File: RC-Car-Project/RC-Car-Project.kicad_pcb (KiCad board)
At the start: 4 copper layers, 80 x 120 mm, 140 parts, among them J1 Conn_01x02_Pin, J10 ANT_IF, J11 Conn_01x02, J12 Conn_01x02, J13 RF_IF, J15 USB4120-03-C_REVA, J2 Conn_01x02_Pin, J3 Conn_01x02_Pin, J4 Conn_01x02_Pin, J5 MCU_IF, J6 Conn_01x02, J7 Conn_01x02, J8 Conn_01x02, J9 Conn_02x09_Odd_Even, Q1 BTN8982TA, Q2 BTN8982TA, Q3 BTN8982TA, Q4 BTN8982TA, Q5 2N7002E, Q6 2N7002E, Q7 PMOS, SW1 SW_Push, U1 LMR16020PDDAR, U11 LMR16030PDDA, U3 STM32H743VGTx, U4 USBLC6-2SC6, U7 INA229AQDGSRQ1, U8 ADC082S021CIMM/NOPB, U9 SN74HC244PWR, Y1 Crystal

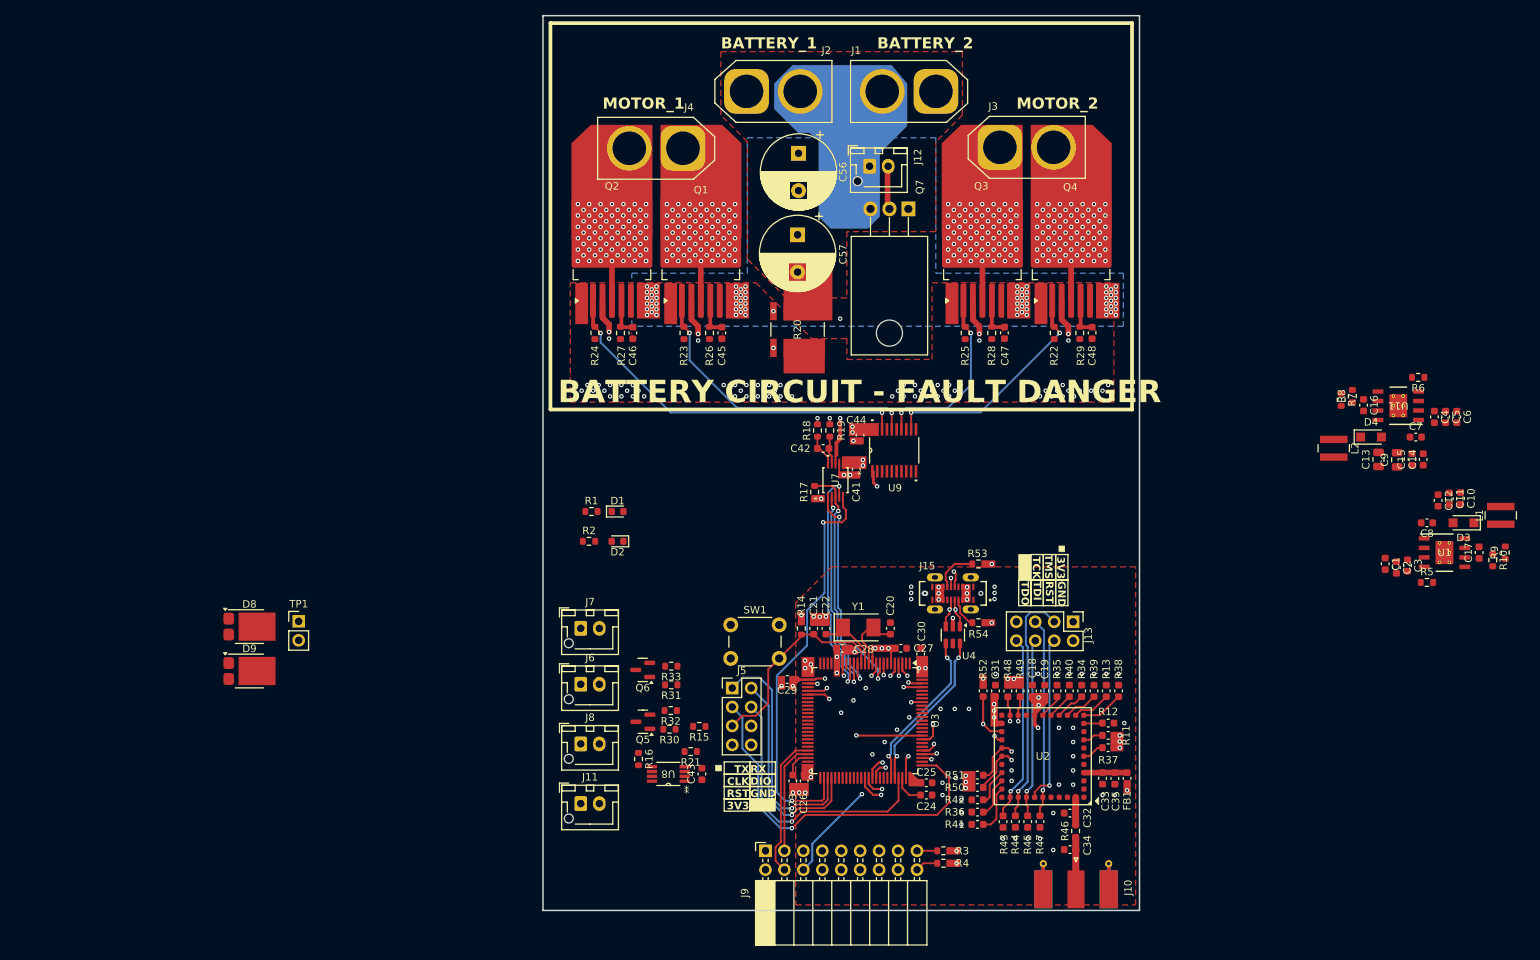
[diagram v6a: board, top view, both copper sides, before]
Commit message: Finished prelim. Car and added screw holes
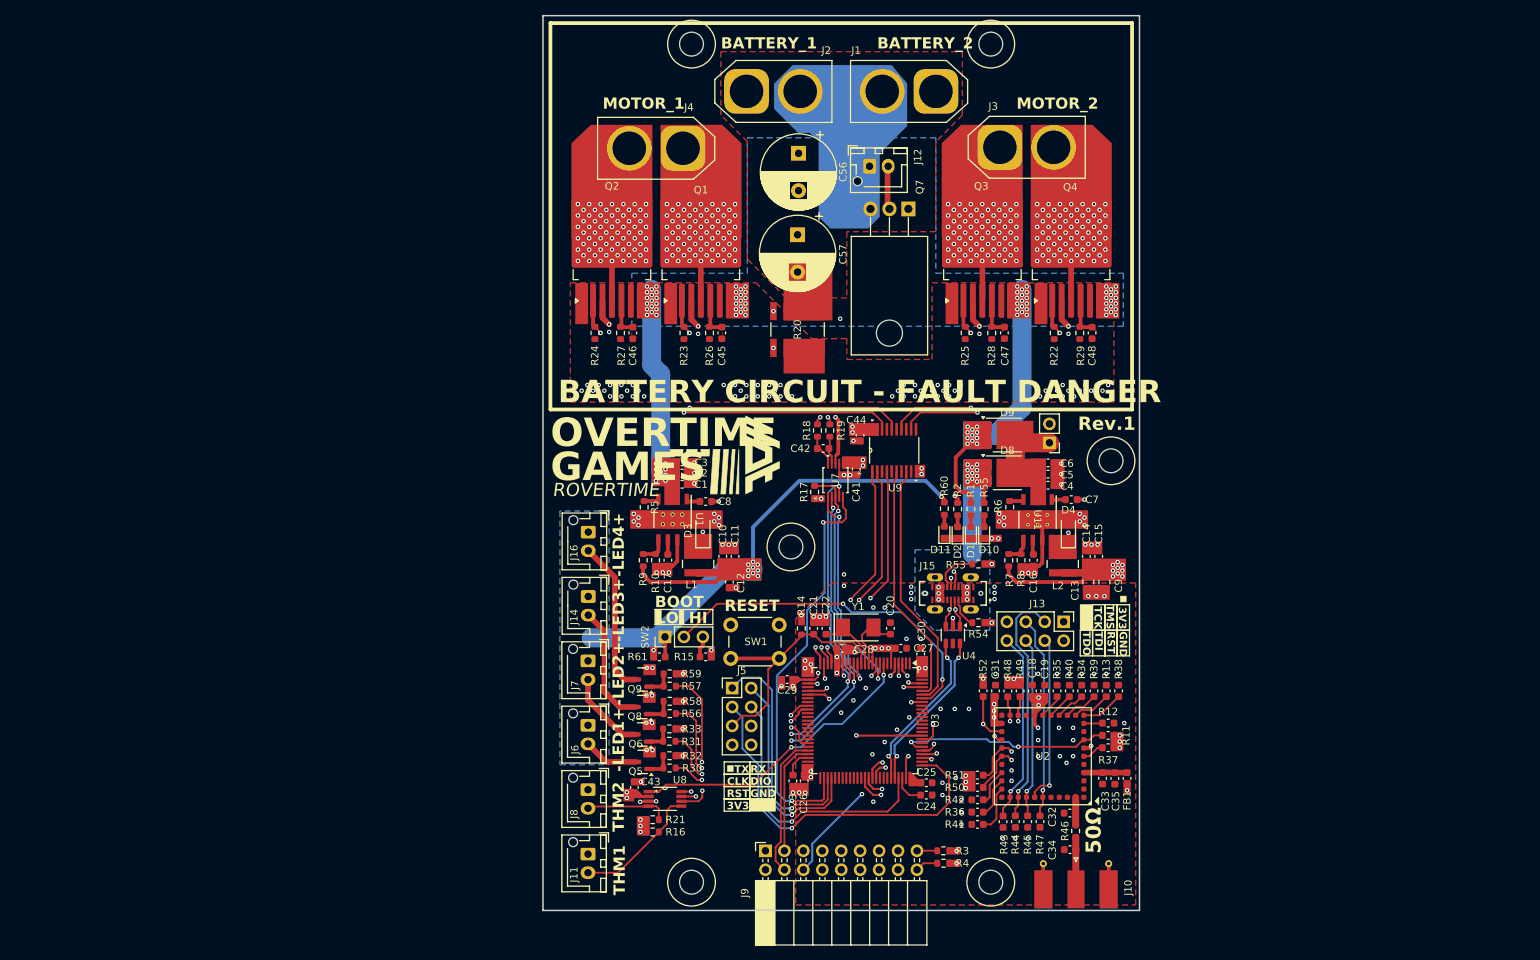
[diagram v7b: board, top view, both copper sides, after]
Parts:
- added D10: LED, LED_SMD:LED_0603_1608Metric, F.Cu at (169.2, 109.3)
- added D11: LED, LED_SMD:LED_0603_1608Metric, F.Cu at (163.8, 109.3)
- added J14: Conn_01x02, Connector_JST:JST_XH_B2B-XH-AM_1x02_P2.50mm_Vertical, F.Cu at (116.1, 117.9)
- added J16: Conn_01x02, Connector_JST:JST_XH_B2B-XH-AM_1x02_P2.50mm_Vertical, F.Cu at (116.1, 109.3)
- added Q8: 2N7002E, Package_TO_SOT_SMD:SOT-23, F.Cu at (123.3, 132.7)
- added Q9: 2N7002E, Package_TO_SOT_SMD:SOT-23, F.Cu at (123.4, 129.0)
- added R55: 220ohm, Resistor_SMD:R_0603_1608Metric, F.Cu at (169.2, 106.2)
- added R56: 100, Resistor_SMD:R_0603_1608Metric, F.Cu at (127.0, 133.6)
- added R57: 100, Resistor_SMD:R_0603_1608Metric, F.Cu at (127.0, 129.9)
- added R58: 10k, Resistor_SMD:R_0603_1608Metric, F.Cu at (127.0, 132.0)
- added R59: 10k, Resistor_SMD:R_0603_1608Metric, F.Cu at (127.0, 128.3)
- added R60: 1.5kohm, Resistor_SMD:R_0603_1608Metric, F.Cu at (163.8, 106.1)
- added R61: 10k, Capacitor_SMD:C_0603_1608Metric, F.Cu at (125.6, 126.0)
- added REF**: MountingHole_3.2mm_M3, MountingHole:MountingHole_3.2mm_M3, F.Cu at (143.3, 111.3)
- added REF**: Overtime_Small, _LOGOS:Overtime_Small, F.Cu at (138.6, 99.1)
- added REF**: MountingHole_3.2mm_M3, MountingHole:MountingHole_3.2mm_M3, F.Cu at (170.1, 43.8)
- added REF**: MountingHole_3.2mm_M3, MountingHole:MountingHole_3.2mm_M3, F.Cu at (170.1, 156.2)
- added REF**: MountingHole_3.2mm_M3, MountingHole:MountingHole_3.2mm_M3, F.Cu at (129.9, 156.2)
- added REF**: MountingHole_3.2mm_M3, MountingHole:MountingHole_3.2mm_M3, F.Cu at (129.9, 43.8)
- added REF**: MountingHole_3.2mm_M3, MountingHole:MountingHole_3.2mm_M3, F.Cu at (186.2, 99.7)
- added SW2: SW_SPDT, Connector_PinHeader_2.54mm:PinHeader_1x03_P2.54mm_Vertical, F.Cu at (126.4, 123.3)
- R15: footprint Resistor_SMD:R_0603_1608Metric -> Capacitor_SMD:C_0603_1608Metric
- moved R9 115.6 mm to (123.4, 113.0), turned to -90 degrees
- moved R10 112.3 mm to (125.1, 113.0), turned to 90 degrees
- moved C17 108.8 mm to (126.7, 113.0), turned to -90 degrees
- moved L1 107.8 mm to (130.8, 113.5), turned to -90 degrees
- moved D9 106.5 mm to (172.3, 96.2)
- moved R5 105.5 mm to (123.6, 105.9), turned to -90 degrees
- moved D8 103.7 mm to (172.3, 101.3)
- moved U1 103.6 mm to (127.4, 107.6), turned to -90 degrees
- moved TP1 103.5 mm to (177.9, 97.3), turned to 180 degrees
- moved D3 102.0 mm to (131.4, 109.1), turned to 90 degrees
- moved C10 99.2 mm to (134.1, 112.5), turned to 90 degrees
- moved C3 98.3 mm to (128.7, 99.8), turned to 0 degrees
- moved C8 96.8 mm to (131.8, 105.2)
- moved C2 96.6 mm to (128.7, 101.3), turned to 0 degrees
- moved C11 96.1 mm to (135.8, 112.5), turned to 90 degrees
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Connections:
- R15 pad 1: Net-(U3-BOOT0) -> Net-(SW2-C)
- R15 pad 2: GNDA -> +3V3
- U3 pad 23: /MCU/MOTOR_EN -> /MCU/RIGHT_PWM1
- U3 pad 24: /MCU/LEFT_PWM2 -> /MCU/LIGHTS4_PWM
- U3 pad 25: unconnected-(U3-PA3-Pad25) -> /MCU/MOTOR_EN
- U3 pad 34: /MCU/LIGHTS2_PWM -> /MCU/LIGHTS3_PWM
- U3 pad 35: unconnected-(U3-PB1-Pad35) -> /MCU/LIGHTS2_PWM
- U3 pad 59: /MCU/RIGHT_PWM1 -> unconnected-(U3-PD12-Pad59)
- U3 pad 89: /MCU/RIGHT_PWM2 -> unconnected-(U3-PB3-Pad89)
- U3 pad 94: Net-(U3-BOOT0) -> Net-(SW2-B)
- U3 pad 95: unconnected-(U3-PB8-Pad95) -> /MCU/RIGHT_PWM2
- U3 pad 96: unconnected-(U3-PB9-Pad96) -> /MCU/LEFT_PWM2
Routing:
- net +12V: track 0.00 -> 76.6 mm, vias 0 -> 10
- net VDD_BATT: track 19.7 -> 79.7 mm, vias 70 -> 92
- net Net-(SW2-B): track 0.00 -> 47.1 mm, vias 0 -> 2
- net /MCU/LIGHTS4_PWM: track 0.00 -> 38.6 mm, vias 0 -> 2
- net /IVTSense/THERMO_ADC_CS: track 1.54 -> 40.1 mm, vias 1 -> 2
- net /MCU/RIGHT_PWM2: track 0.00 -> 33.7 mm
- net /MCU/LEFT_PWM2: track 0.00 -> 32.6 mm
- net /IVTSense/MOSI: track 28.7 -> 60.3 mm, vias 2 -> 4
- net /IVTSense/MISO: track 32.3 -> 63.9 mm, vias 2 -> 4
- net /MCU/RIGHT_PWM1: track 0.00 -> 29.7 mm, vias 0 -> 2
- net /MCU/LEFT_PWM1: track 0.00 -> 29.4 mm, vias 0 -> 2
- net /MCU/LIGHTS3_PWM: track 0.00 -> 29.4 mm, vias 0 -> 2
- net /MCU/MOTOR_EN: track 2.22 -> 29.5 mm, vias 1 -> 2
- net /MCU/LIGHTS2_PWM: track 0.00 -> 26.4 mm, vias 0 -> 2
- net /MCU/RF_RESET: track 2.73 -> 28.6 mm, vias 0 -> 2
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- added copper zone on B.Cu, net +12V
- added copper zone on B.Cu, net VDD_USB
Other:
- board text added: "-LED1+"
- board text added: "-LED2+"
- board text added: "-LED3+"
- board text added: "-LED4+"
- board text added: "50Ω"
- board text added: "BOOT"
- board text added: "GAMES"
- board text added: "HI"
- board text added: "LO"
- board text added: "OVERTIME"
- board text added: "RESET"
- board text added: "ROVERTIME"
- board text added: "Rev.1"
- board text added: "THM1"
- board text added: "THM2"

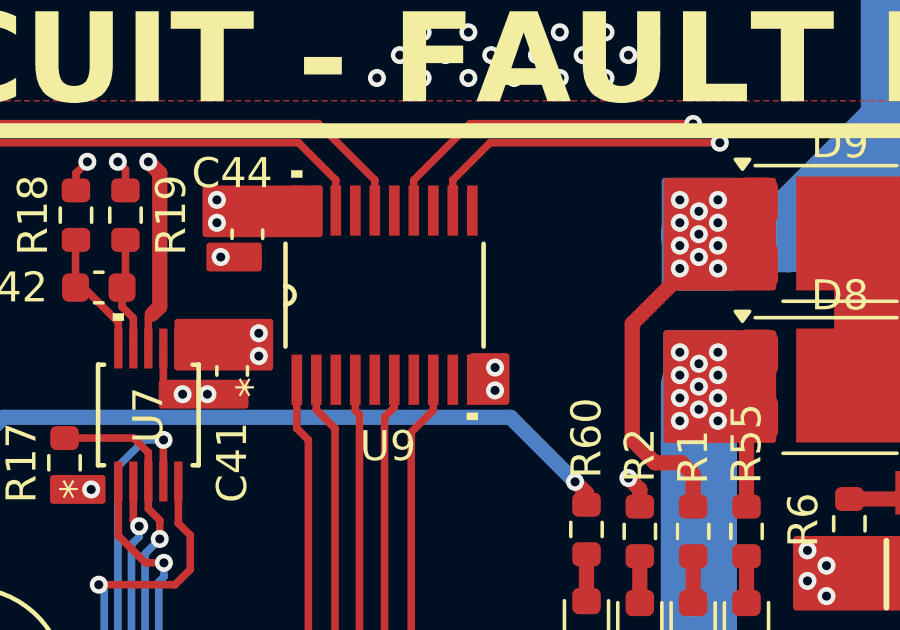
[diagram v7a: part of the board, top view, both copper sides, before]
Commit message: Redid Screwholes
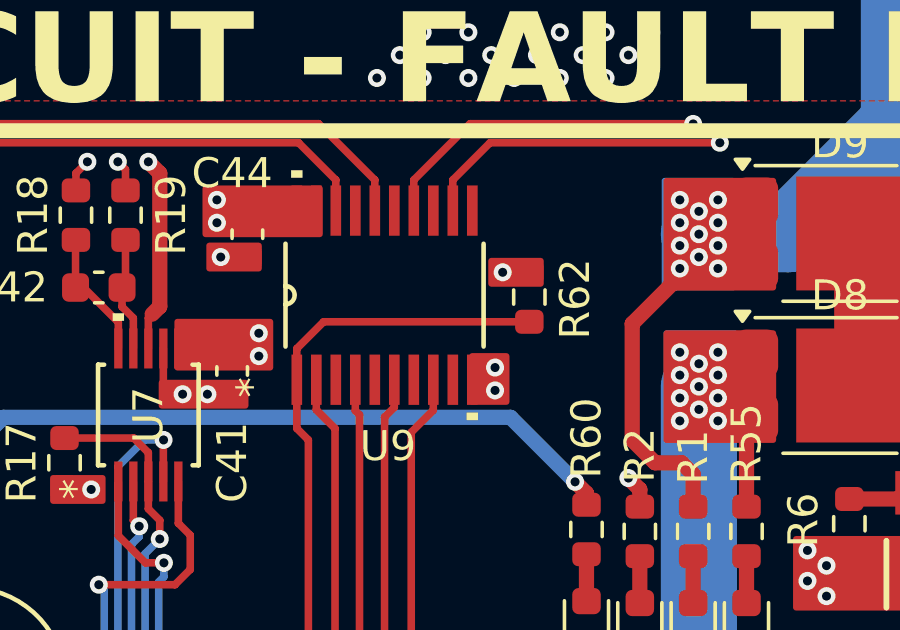
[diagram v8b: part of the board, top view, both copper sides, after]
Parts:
- added R62: 10k, Resistor_SMD:R_0603_1608Metric, F.Cu at (161.9, 98.4)
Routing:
- net /MCU/MOTOR_EN: track 29.5 -> 38.7 mm
- net +3V3: vias 55 -> 56
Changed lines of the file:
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@@
 		)
 	)
+	(footprint "Resistor_SMD:R_0603_1608Metric"
+		(layer "F.Cu")
+		(at 161.925 98.361 90)
+		(descr "Resistor SMD 0603 (1608 Metric), square (rectangular) end terminal, IPC_7351 nominal, (Body size source: IPC-SM-782 page 72, https://www.pcb-3d.com/wordpress/wp-content/uploads/ipc-sm-782a_amendment_1_and_2.pdf), generated with kicad-footprint-generator")
+		(tags "resistor")
+		(property "Reference" "R62"
+			(at -0.064 1.524 90)
+			(layer "F.SilkS")
+			(effects
+				(font
+					(size 1 1)
+					(thickness 0.15)
+				)
+			)
+		)
+		(property "Value" "10k"
+			(at 0 1.43 90)
+			(layer "F.Fab")
+			(effects
+				(font
+					(size 1 1)
+					(thickness 0.15)
+				)
+			)
+		)
+		(property "Footprint" "Resistor_SMD:R_0603_1608Metric"
+			(at 0 0 90)
+			(unlocked yes)
+			(layer "F.Fab")
+			(hide yes)
+			(effects
+				(font
+					(size 1.27 1.27)
+					(thickness 0.15)
+				)
+			)
+		)
+		(property "Datasheet" ""
+			(at 0 0 90)
+			(unlocked yes)
+			(layer "F.Fab")
+			(hide yes)
+			(effects
+				(font
+					(size 1.27 1.27)
+					(thickness 0.15)
+				)
+			)
+		)
+		(property "Description" "Resistor"
+			(at 0 0 90)
+			(unlocked yes)
+			(layer "F.Fab")
+			(hide yes)
+			(effects
+				(font
+					(size 1.27 1.27)
+					(thickness 0.15)
+				)
+			)
+		)
+		(property ki_fp_filters "R_*")
+		(sheetname "MotorDriver")
+		(sheetfile "MotorDriver.kicad_sch")
+		(attr smd)
+		(fp_line
+			(start -0.237258 -0.5225)
+			(end 0.237258 -0.5225)
+			(stroke
+				(width 0.12)
+				(type solid)
+			)
+			(layer "F.SilkS")
+		)
+		(fp_line
+			(start -0.237258 0.5225)
+			(end 0.237258 0.5225)
+			(stroke
+				(width 0.12)
+				(type solid)
+			)
+			(layer "F.SilkS")
+		)
+		(fp_line
+			(start 1.48 -0.73)
+			(end 1.48 0.73)
+			(stroke
+				(width 0.05)
+				(type solid)
+			)
+			(layer "F.CrtYd")
+		)
+		(fp_line
+			(start -1.48 -0.73)
+			(end 1.48 -0.73)
+			(stroke
+				(width 0.05)
+				(type solid)
+			)
+			(layer "F.CrtYd")
+		)
+		(fp_line
+			(start 1.48 0.73)
+			(end -1.48 0.73)
+			(stroke
+				(width 0.05)
+				(type solid)
+			)
+			(layer "F.CrtYd")
+		)
+		(fp_line
+			(start -1.48 0.73)
+			(end -1.48 -0.73)
+			(stroke
+				(width 0.05)
+				(type solid)
+			)
+			(layer "F.CrtYd")
+		)
+		(fp_line
+			(start 0.8 -0.4125)
+			(end 0.8 0.4125)
+			(stroke
+				(width 0.1)
+				(type solid)
+			)
+			(layer "F.Fab")
+		)
+		(fp_line
+			(start -0.8 -0.4125)
+			(end 0.8 -0.4125)
+			(stroke
+				(width 0.1)
+				(type solid)
+			)
+			(layer "F.Fab")
+		)
+		(fp_line
+			(start 0.8 0.4125)
+			(end -0.8 0.4125)
+			(stroke
+				(width 0.1)
+				(type solid)
+			)
+			(layer "F.Fab")
+		)
+		(fp_line
+			(start -0.8 0.4125)
+			(end -0.8 -0.4125)
+			(stroke
+				(width 0.1)
+				(type solid)
+			)
+			(layer "F.Fab")
+		)
+		(fp_text user "${REFERENCE}"
+			(at 0 0 90)
+			(layer "F.Fab")
+			(effects
+				(font
+					(size 0.4 0.4)
+					(thickness 0.06)
+				)
+			)
+		)
+		(pad "1" smd roundrect
+			(at -0.825 0 90)
+			(size 0.8 0.95)
+			(layers "F.Cu" "F.Paste" "F.Mask")
+			(roundrect_rratio 0.25)
+			(net 46 "/MCU/MOTOR_EN")
+			(pintype "passive")
+		)
+		(pad "2" smd roundrect
+			(at 0.825 0 90)
+			(size 0.8 0.95)
+			(layers "F.Cu" "F.Paste" "F.Mask")
+			(roundrect_rratio 0.25)
+			(net 3 "+3V3")
+			(pintype "passive")
+		)
+		(model "${KICAD8_3DMODEL_DIR}/Resistor_SMD.3dshapes/R_0603_1608Metric.wrl"
+			(offset
+				(xyz 0 0 0)
+			)
+			(scale
+				(xyz 1 1 1)
+			)
+			(rotate
+				(xyz 0 0 0)
+			)
+		)
+	)
 	(footprint "MountingHole:MountingHole_3.2mm_M3"
 		(layer "F.Cu")
@@
 	)
 	(gr_rect
+		(start 160.655 97.155)
+		(end 162.306 97.917)
+		(stroke
+			(width 0.2)
+			(type solid)
+		)
+		(fill solid)
+		(layer "F.Cu")
+		(net 3)
+	)
+	(gr_rect
 		(start 123.48114 134.441927)
 		(end 125.00514 135.711927)
@@
 	)
 	(via
+		(at 161.036 97.536)
+		(size 0.6)
+		(drill 0.3)
+		(layers "F.Cu" "B.Cu")
+		(net 3)
+	)
+	(via
 		(at 187.071 114.046)
 		(size 0.6)
@@
 	)
 	(segment
+		(start 155.068 99.186)
+		(end 161.925 99.186)
+		(width 0.254)
+		(layer "F.Cu")
+		(net 46)
+	)
+	(segment
 		(start 146.551915 124.714)
 		(end 146.551915 125.215915)
@@
 	)
 	(segment
+		(start 154.174 101.1174)
+		(end 154.174 100.08)
+		(width 0.254)
+		(layer "F.Cu")
+		(net 46)
+	)
+	(segment
 		(start 147.186 125.85)
 		(end 147.186 126.873)
@@
 		(width 0.254)
 		(layer "F.Cu")
+		(net 46)
+	)
+	(segment
+		(start 154.174 100.08)
+		(end 155.068 99.186)
+		(width 0.254)
+		(layer "F.Cu")
